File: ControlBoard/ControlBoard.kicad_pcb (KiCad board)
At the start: 2 copper layers, 144 x 106 mm, 168 parts, among them J1 PowerIn, J10 Conn_01x01, J11 Conn_01x01, J12 Conn_01x01, J13 Conn_01x01, J14 Conn_01x01, J15 Conn_01x01, J16 Conn_01x06, J17 Conn_01x06, J18 Conn_01x06, J2 UART, J3 ICSP, J4 MTR1, J5 MTR2, J6 Ultrasonic Transmitter, J7 Ultrasonic Receiver, J8 Conn_01x01, J9 Conn_01x01, Q1 2N3904, Q2 2N3904, SW1 SW_Push, U1 LM358, U10 LMT85, U11 74HC138, U12 4051, U13 4051, U2 LM358, U3 LM358, U4 LM358, U5 ATMEGA328P-PU, U6 LM7805_TO220, U7 74HC595, U8 L298D, U9 74HC595, Y1 16MHz

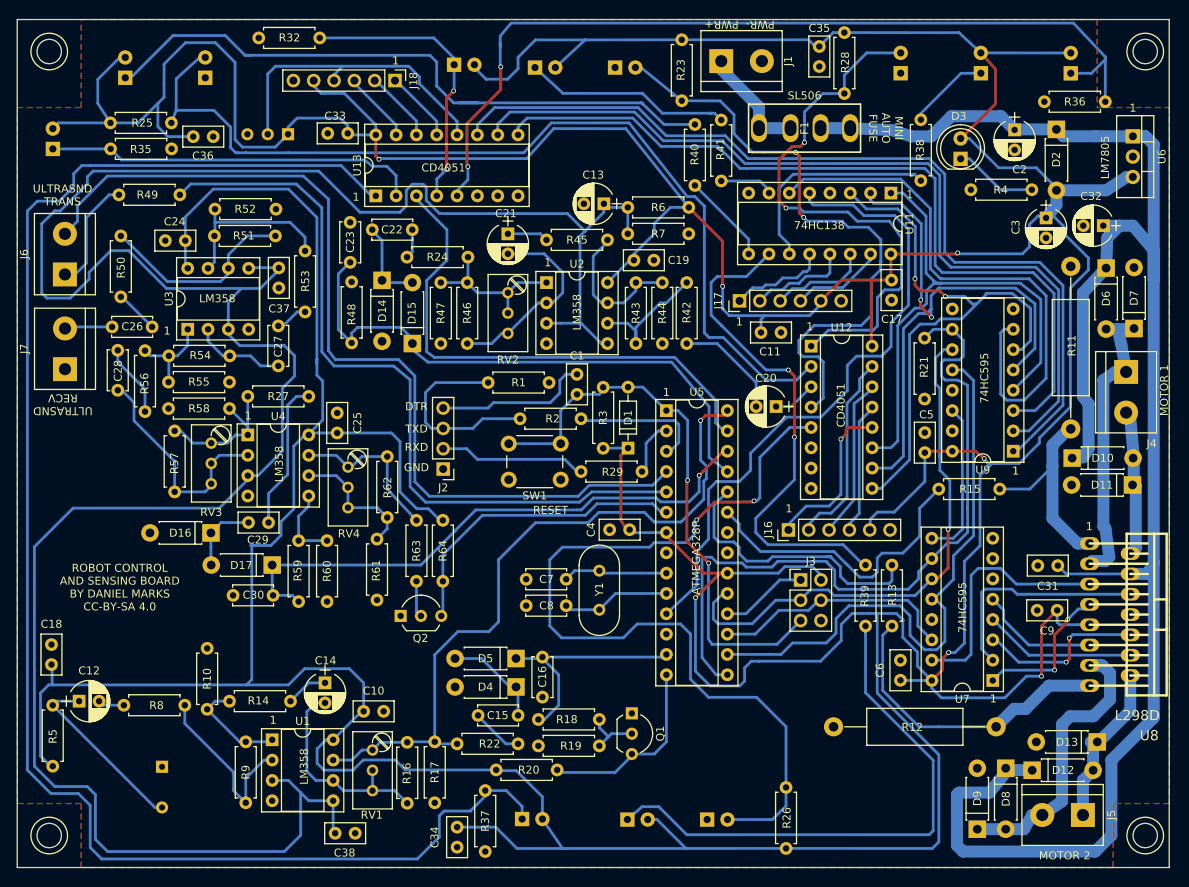
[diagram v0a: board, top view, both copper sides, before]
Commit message: Added CAD models
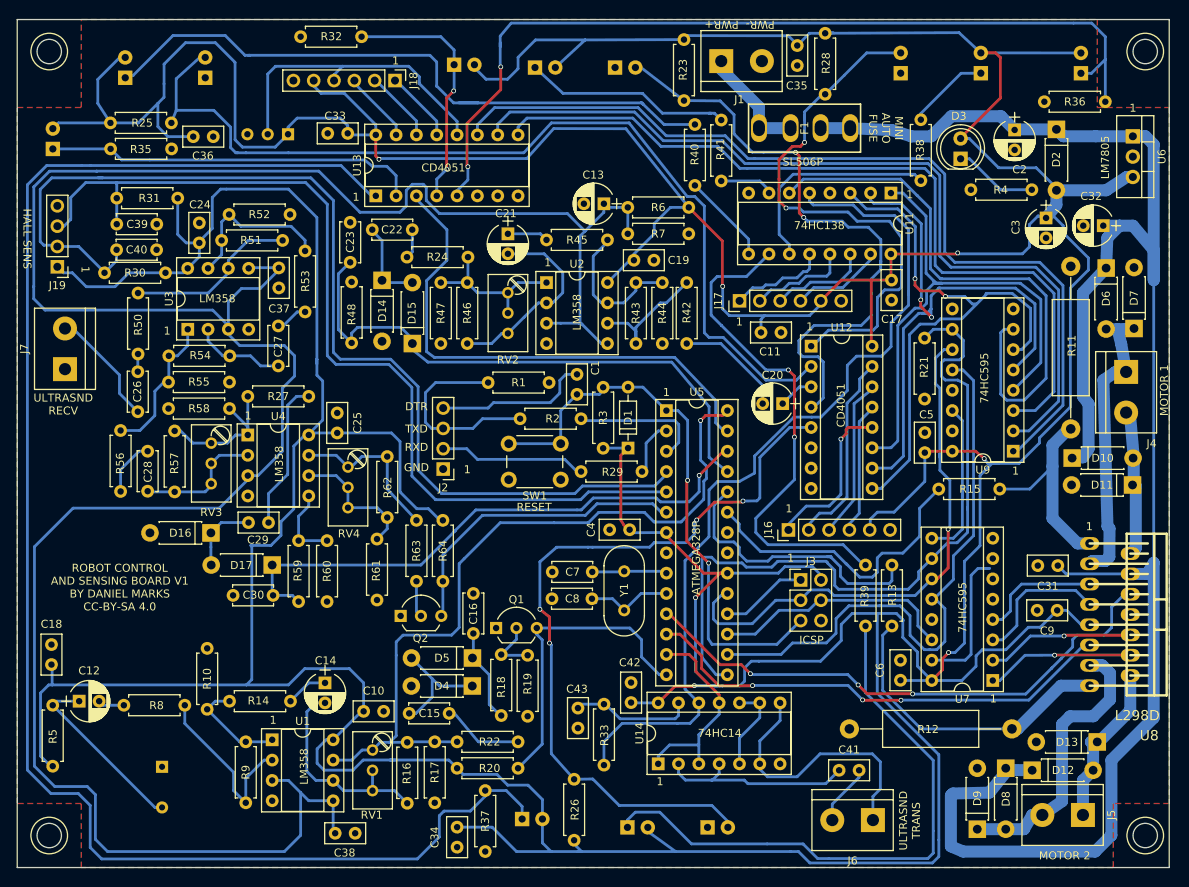
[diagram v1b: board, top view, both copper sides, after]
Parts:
- removed R49: 0R, Resistors_THT:R_Axial_DIN0207_L6.3mm_D2.5mm_P7.62mm_Horizontal
- added C39: 100 pF, Capacitors_THT:C_Disc_D5.0mm_W2.5mm_P5.00mm, F.Cu at (67.4, 64.6)
- added C40: 100 pF, Capacitors_THT:C_Disc_D5.0mm_W2.5mm_P5.00mm, F.Cu at (67.4, 67.8)
- added C41: 100 nF, Capacitors_THT:C_Disc_D5.0mm_W2.5mm_P2.50mm, F.Cu at (157.7, 132.8)
- added C42: 100 nF, Capacitors_THT:C_Disc_D5.0mm_W2.5mm_P2.50mm, F.Cu at (131.7, 124.4)
- added C43: 100 nF, Capacitors_THT:C_Disc_D5.0mm_W2.5mm_P2.50mm, F.Cu at (125.1, 125.1)
- added J19: HALLSENS, Pin_Headers:Pin_Header_Straight_1x04_Pitch2.54mm, F.Cu at (60.0, 69.9)
- added R30: 10k, Resistors_THT:R_Axial_DIN0207_L6.3mm_D2.5mm_P7.62mm_Horizontal, F.Cu at (65.9, 70.7)
- added R31: 10k, Resistors_THT:R_Axial_DIN0207_L6.3mm_D2.5mm_P7.62mm_Horizontal, F.Cu at (67.4, 61.3)
- added R33: 10k, Resistors_THT:R_Axial_DIN0207_L6.3mm_D2.5mm_P7.62mm_Horizontal, F.Cu at (128.3, 132.2)
- added U14: 74HC14, Housings_DIP:DIP-14_W7.62mm_Socket, F.Cu at (135.1, 132.0)
- F1: value SL506 -> SL506P
- R10, R29, R44: value 10k -> 1k
- moved J6 121.9 mm to (162.0, 139.1), turned to 180 degrees
- moved R26 26.5 mm to (124.6, 134.0)
- moved Q1 20.0 mm to (114.9, 115.1), turned to 0 degrees
- moved C16 15.6 mm to (112.0, 110.7), turned to 270 degrees
- moved R18 14.7 mm to (115.5, 118.4), turned to 270 degrees
- moved C15 13.6 mm to (104.0, 125.7), turned to 0 degrees
- moved C28 13.2 mm to (71.3, 98.0)
- moved R56 10.4 mm to (67.9, 98.0)
- moved R50 7.46 mm to (70.1, 73.2)
- moved C26 5.88 mm to (70.1, 83.0), turned to 270 degrees
- moved D4 5.47 mm to (111.9, 122.3)
- moved D5 5.45 mm to (111.9, 118.8)
- moved R32 5.24 mm to (90.4, 41.1)
- moved R20 4.89 mm to (117.6, 132.6)
- moved R19 3.94 mm to (118.8, 126.1), turned to 90 degrees
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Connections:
- C16 pad 2: MICPEAKOUT -> Net-(C16-Pad2)
- D5 pad 1: MICPEAKOUT -> Net-(C16-Pad2)
- J6 pad 2: ULTRATRANS1 -> Net-(C41-Pad2)
- R18 pad 2: MICPEAKOUT -> Net-(C16-Pad2)
- U5 pad 11: PHOTSIG -> MOTORPWM1
- U5 pad 12: Net-(U5-Pad12) -> MOTORPWM2
- U5 pad 13: MICPEAKOUT -> ULTRATRANS
- U5 pad 4: ULTRATRANS1 -> Net-(C40-Pad1)
- U5 pad 5: ULTRATRANS2 -> Net-(C39-Pad1)
- U7 pad 1: MTRIN2 -> MTRIN4
- U7 pad 15: MTRIN1 -> Net-(U7-Pad15)
- U7 pad 2: MTRENA -> MTRIN3
- U7 pad 3: MTRIN3 -> MTRIN2
- U7 pad 4: MTRIN4 -> MTRIN1
- U7 pad 5: MTRENB -> Net-(U7-Pad5)
- U8 pad 11: MTRENB -> MOTORPWM2
- U8 pad 6: MTRENA -> MOTORPWM1
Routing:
- net Net-(C40-Pad1): track 0.00 -> 134.1 mm
- net Net-(C39-Pad1): track 0.00 -> 119.8 mm
- net ULTRATRANS1: track 116.0 -> 0.00 mm
- net ULTRATRANS2: track 96.6 -> 0.00 mm
- net MOTORPWM1: track 0.00 -> 69.5 mm, vias 0 -> 3
- net MOTORPWM2: track 0.00 -> 60.2 mm, vias 0 -> 3
- net +5V: track 918.4 -> 957.7 mm
- net MICPEAKOUT: track 29.1 -> 0.00 mm
- net PHOTSIG: track 82.7 -> 111.0 mm
- net MTRENA: track 28.1 -> 0.00 mm
- net ULTRATRANS: track 0.00 -> 26.0 mm
- net Net-(C41-Pad1): track 0.00 -> 25.0 mm
- net Net-(J6-Pad1): track 14.2 -> 34.8 mm
- net Net-(U7-Pad15): track 0.00 -> 18.2 mm
- net MTRIN1: track 32.1 -> 16.4 mm
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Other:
- board text added: "74HC14"
- board text added: "HALL SENS"
- board text added: "ICSP"
- board text added: "ROBOT CONTROL AND SENSING BOARD V1 BY DANIEL MARKS CC-BY-SA 4.0"
- board text added: "SL506P"
- board text removed: "ROBOT CONTROL AND SENSING BOARD BY DANIEL MARKS CC-BY-SA 4.0"
- board text removed: "SL506"

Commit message: Added KeypadPI
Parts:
- added C44: 100 pF, Capacitors_THT:C_Disc_D5.0mm_W2.5mm_P5.00mm, F.Cu at (125.3, 120.9)
- added C45: 100 pF, Capacitors_THT:C_Disc_D5.0mm_W2.5mm_P5.00mm, F.Cu at (118.7, 120.9)
- added C46: 100 nF, Capacitors_THT:C_Disc_D5.0mm_W2.5mm_P2.50mm, F.Cu at (168.4, 89.2)
- added J20: Conn_01x06, Pin_Headers:Pin_Header_Straight_1x06_Pitch2.54mm, F.Cu at (178.4, 126.3)
- added J21: HALLSENS2, Pin_Headers:Pin_Header_Straight_1x04_Pitch2.54mm, F.Cu at (118.4, 115.8)
- added R34: 10k, Resistors_THT:R_Axial_DIN0207_L6.3mm_D2.5mm_P7.62mm_Horizontal, F.Cu at (128.5, 120.8)
- added R49: 10k, Resistors_THT:R_Axial_DIN0207_L6.3mm_D2.5mm_P7.62mm_Horizontal, F.Cu at (122.0, 120.9)
- added R65: 10k, Resistors_THT:R_Axial_DIN0207_L6.3mm_D2.5mm_P7.62mm_Horizontal, F.Cu at (111.7, 108.5)
- R51, R54: value 100k -> 220k
- R63: value 10k -> 1k
- moved R26 30.6 mm to (155.2, 134.8)
- moved C16 17.8 mm to (94.8, 115.2), turned to 0 degrees
- moved R10 11.2 mm to (68.3, 121.5), turned to 0 degrees
- moved C14 11.1 mm to (82.5, 120.2), turned to 0 degrees
- moved C43 9.40 mm to (121.2, 133.6), turned to 90 degrees
- moved R18 9.19 mm to (111.0, 126.4), turned to 90 degrees
- moved C15 7.47 mm to (96.5, 125.3)
- moved D4 7.45 mm to (104.4, 122.0)
- moved D5 7.44 mm to (104.5, 118.5)
- moved C10 6.41 mm to (92.0, 124.2), turned to 180 degrees
- moved C41 5.34 mm to (153.9, 129.1), turned to 270 degrees
- moved R12 3.70 mm to (177.6, 130.9)
- moved R22 3.62 mm to (107.8, 126.4), turned to 90 degrees
- moved R14 3.36 mm to (78.2, 124.7)
- moved R19 3.29 mm to (117.6, 129.2), turned to 180 degrees
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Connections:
- J3 pad 1: MISO -> MICTHR
- Q1 pad 3: MICTHR -> Net-(Q1-Pad3)
- R20 pad 1: MICTHR -> Net-(Q1-Pad3)
- R21 pad 1: CLROUT -> +5V
- R21 pad 2: GND -> CLROUT
- U5 pad 14: MICTHR -> Net-(C45-Pad1)
- U5 pad 15: CLROUT -> Net-(C44-Pad1)
- U5 pad 18: MISO -> MICTHR
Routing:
- net +5V: track 957.7 -> 1020.9 mm
- net CLROUT: track 91.9 -> 51.2 mm
- net Net-(C44-Pad1): track 0.00 -> 31.4 mm, vias 0 -> 2
- net Net-(Q1-Pad3): track 0.00 -> 29.6 mm
- net Net-(PT2-Pad2): track 96.4 -> 124.1 mm, vias 4 -> 2
- net Net-(C45-Pad1): track 0.00 -> 26.6 mm
- net Net-(J20-Pad4): track 0.00 -> 23.8 mm
- net Net-(J20-Pad3): track 0.00 -> 20.2 mm
- net Net-(J20-Pad2): track 0.00 -> 17.5 mm
- net MICOUT: track 95.3 -> 111.3 mm
- net Net-(Q1-Pad2): track 7.44 -> 18.4 mm
- net MISO: track 10.9 -> 0.00 mm
- net Net-(J20-Pad5): track 18.2 -> 9.03 mm
- net Net-(R12-Pad1): track 39.3 -> 46.5 mm
- net Net-(C43-Pad1): track 15.3 -> 22.2 mm
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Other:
- board text added: "HALL SENS 2"

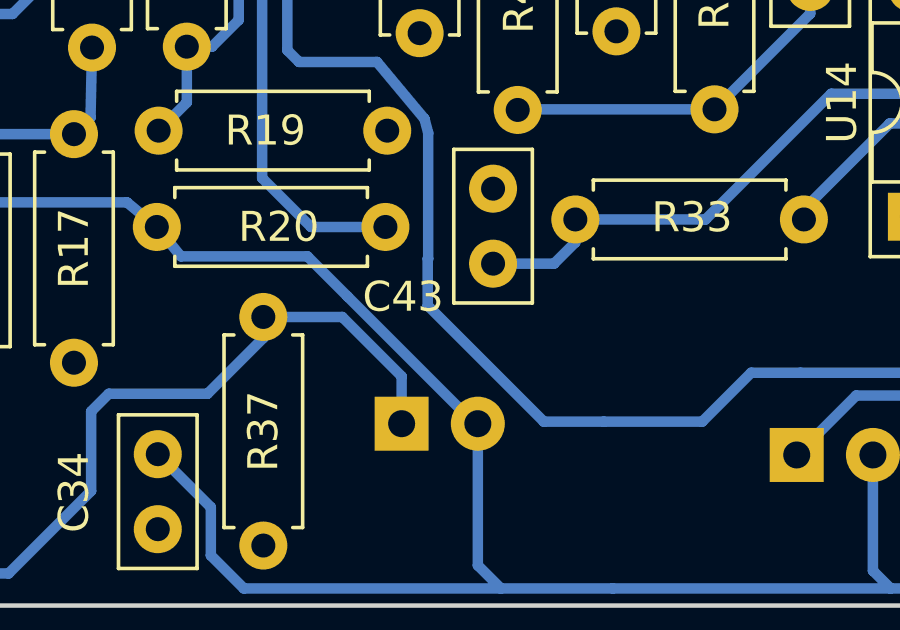
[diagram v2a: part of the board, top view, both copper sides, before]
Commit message: Added audio input and output to keypad PCB
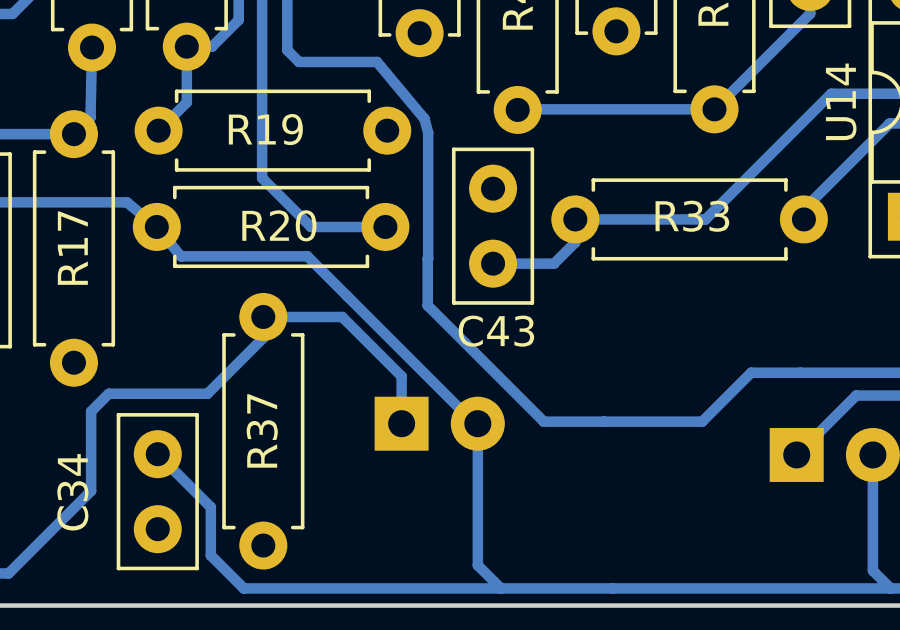
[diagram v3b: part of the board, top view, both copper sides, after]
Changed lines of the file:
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@@
     (links 409)
     (no_connects 0)
-    (area 54.924999 38.924999 199.075001 145.075001)
+    (area 54.252381 38.749 200.74762 145.335)
     (thickness 1.6)
     (drawings 54)
@@
   )
   (setup
-    (last_trace_width 0.35)
+    (last_trace_width 0.25)
     (user_trace_width 0.35)
     (user_trace_width 0.5)
@@
     (descr "C, Disc series, Radial, pin pitch=2.50mm, , diameter*width=5*2.5mm^2, Capacitor, http://cdn-reichelt.de/documents/datenblatt/B300/DS_KERKO_TC.pdf")
     (tags "C Disc series Radial pin pitch 2.50mm  diameter 5mm width 2.5mm Capacitor")
-    (fp_text reference C43 (at -1.106 -2.998 180) (layer F.SilkS)
+    (fp_text reference C43 (at -2.286 0.127 180) (layer F.SilkS)
       (effects (font (size 1 1) (thickness 0.15)))
     )

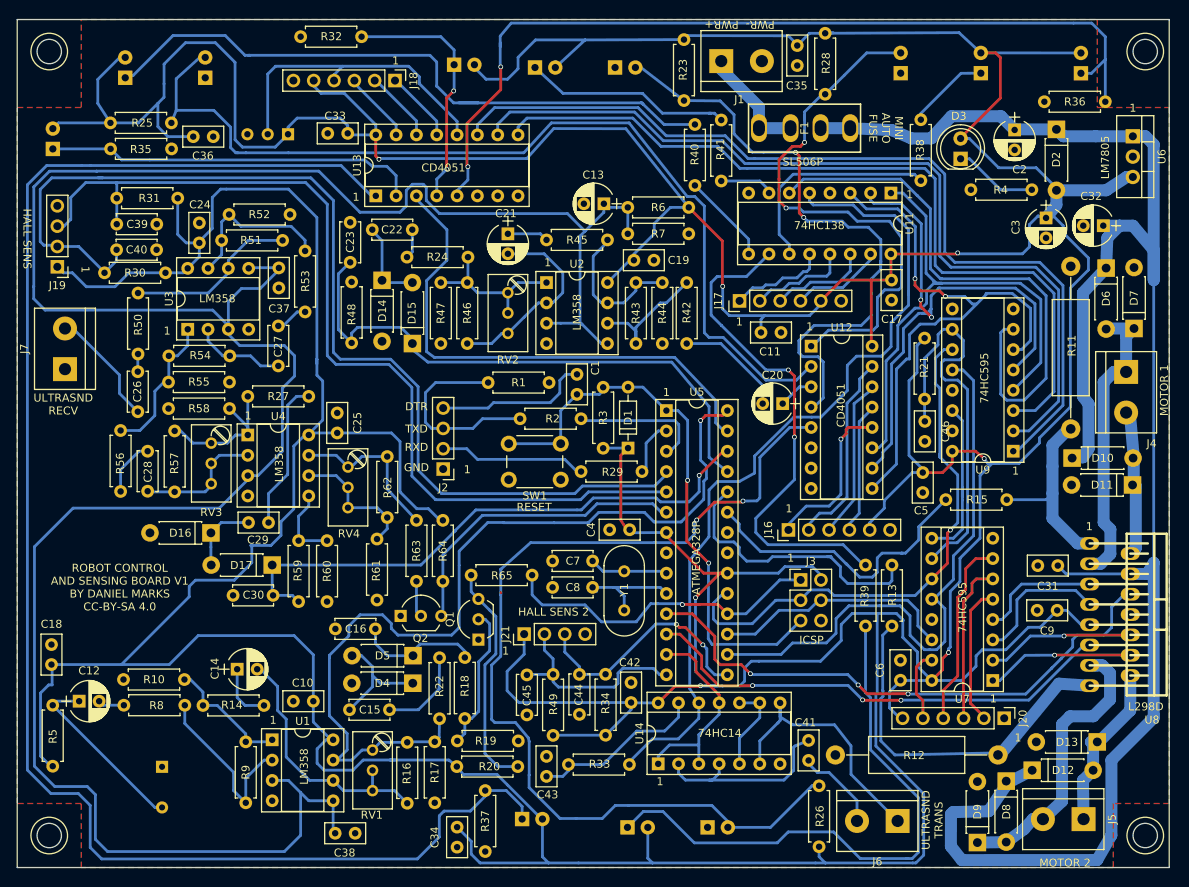
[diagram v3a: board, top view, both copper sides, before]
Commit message: Added second microphone to keypad
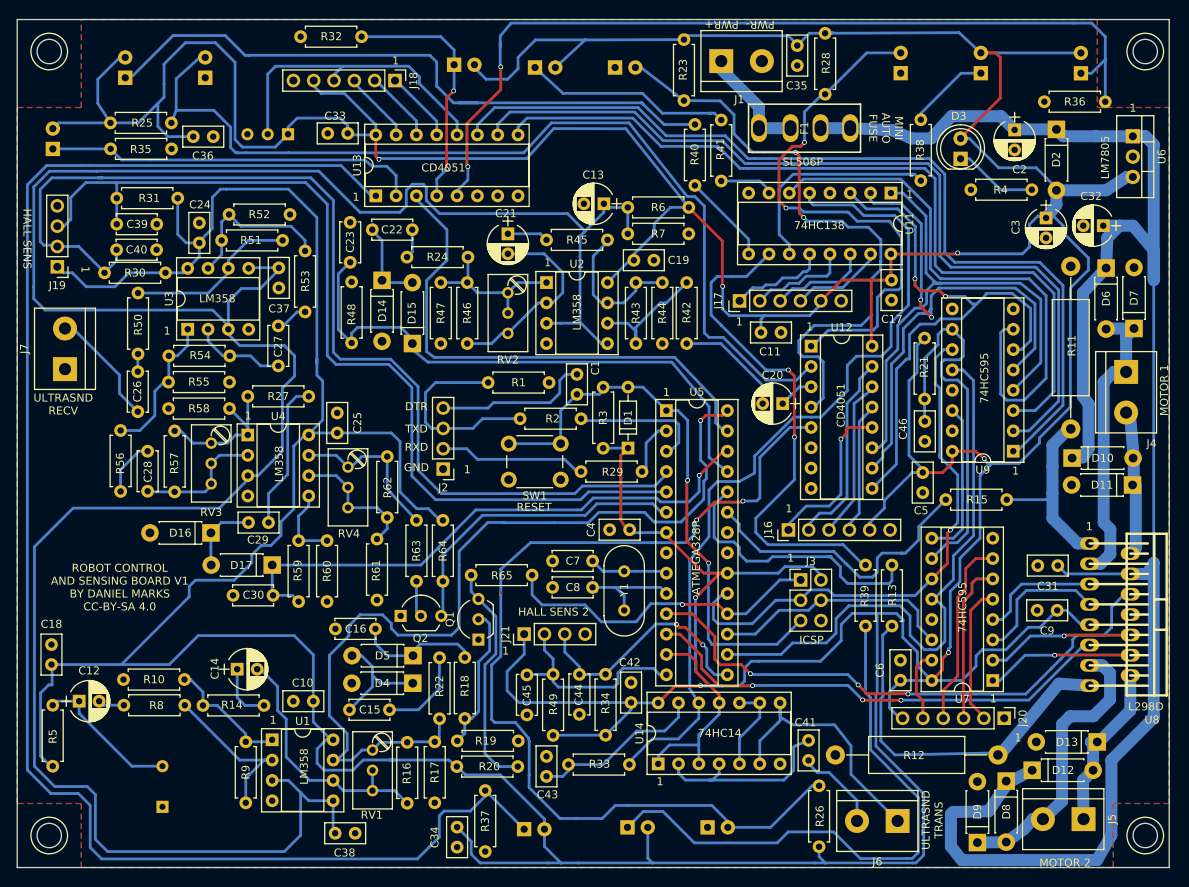
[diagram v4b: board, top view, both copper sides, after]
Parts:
- moved PDT1 1.30 mm to (118.4, 140.2)
- moved MK1 0.09 mm to (73.2, 134.9), turned to 0 degrees
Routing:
- net Net-(C12-Pad1): track 22.6 -> 18.2 mm
- net Net-(R8-Pad1): track 22.6 -> 21.1 mm

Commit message: A few fixes
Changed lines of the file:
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@@
     (thickness 1.6)
     (drawings 54)
-    (tracks 1942)
+    (tracks 1943)
     (zones 0)
     (modules 185)
@@
   )
   (setup
-    (last_trace_width 0.35)
+    (last_trace_width 1.5)
     (user_trace_width 0.35)
     (user_trace_width 0.5)
@@
   (segment (start 123.568 83.352) (end 122.82 84.1) (width 0.35) (layer B.Cu) (net 2))
   (segment (start 124.718 83.102) (end 124.968 83.352) (width 0.35) (layer B.Cu) (net 2) (status 30))
+  (segment (start 197.06 107) (end 197.06 71.575) (width 1.5) (layer B.Cu) (net 3))
   (segment (start 194.13 108.3) (end 186.11 108.3) (width 0.35) (layer B.Cu) (net 3))
   (segment (start 186.11 108.3) (end 185.07 107.26) (width 0.35) (layer B.Cu) (net 3))
@@
   (segment (start 185.764 53.594) (end 184.9 52.73) (width 1.5) (layer B.Cu) (net 3))
   (segment (start 197.06 71.575) (end 197.06 54.635) (width 1.5) (layer B.Cu) (net 3))
-  (segment (start 196.019 53.594) (end 194.45 53.6) (width 1.5) (layer B.Cu) (net 3) (status 20))
   (segment (start 197.06 54.635) (end 196.019 53.594) (width 1.5) (layer B.Cu) (net 3))
+  (segment (start 196.019 53.594) (end 194.45 53.6) (width 1.5) (layer B.Cu) (net 3) (status 20))
   (segment (start 189.794 53.594) (end 194.45 53.6) (width 1.5) (layer B.Cu) (net 3) (status 20))
   (segment (start 197.06 125.984) (end 197.06 126.282) (width 1.5) (layer B.Cu) (net 3))
@@
   (segment (start 173.067762 144.070539) (end 189.988 144.062) (width 1.5) (layer B.Cu) (net 3))
   (segment (start 189.988 144.062) (end 191.77 140.97) (width 1.5) (layer B.Cu) (net 3))
-  (segment (start 197.06 125.984) (end 197.06 106.91) (width 1.5) (layer B.Cu) (net 3))
+  (segment (start 197.06 125.984) (end 197.06 107) (width 1.5) (layer B.Cu) (net 3))
+  (segment (start 197.06 107) (end 197.06 106.91) (width 1.5) (layer B.Cu) (net 3))
   (segment (start 181.864 132.842) (end 178.832 134.412) (width 1.5) (layer B.Cu) (net 3) (status 20))
   (segment (start 178.832 134.412) (end 178.62 134.2) (width 1.5) (layer B.Cu) (net 3) (status 30))
   (segment (start 194.13 108.3) (end 196.25 108.3) (width 1.5) (layer B.Cu) (net 3))
   (segment (start 197.06 67.84) (end 194.47 64.77) (width 1.5) (layer B.Cu) (net 3))
-  (segment (start 197.06 106.91) (end 197.06 71.575) (width 0.35) (layer B.Cu) (net 3))
+  (segment (start 194.47 64.77) (end 192.786 64.77) (width 1.5) (layer B.Cu) (net 3))
   (segment (start 197.06 71.575) (end 197.06 67.84) (width 1.5) (layer B.Cu) (net 3))
   (segment (start 196.25 108.3) (end 197.06 106.91) (width 1.5) (layer B.Cu) (net 3))
@@
   (segment (start 191.262 66.294) (end 192.786 64.77) (width 1.5) (layer B.Cu) (net 3))
   (segment (start 194.45 53.6) (end 195.212 53.6) (width 1.5) (layer B.Cu) (net 3) (status 30))
-  (segment (start 194.47 64.77) (end 192.786 64.77) (width 1.5) (layer B.Cu) (net 3))
   (segment (start 192.786 64.77) (end 190.754 64.77) (width 1.5) (layer B.Cu) (net 3))
   (segment (start 185.07 107.26) (end 185.47 107.26) (width 0.35) (layer B.Cu) (net 3) (status 30))

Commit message: JLCPCB order 2021-10-03
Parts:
- added C47: 100 uF, Capacitors_THT:CP_Radial_D5.0mm_P2.50mm, F.Cu at (72.1, 111.2)
- added J22: PowerIn, Connectors_Terminal_Blocks:TerminalBlock_bornier-2_P5.08mm, F.Cu at (59.4, 116.1)
- R23, R25, R26, R28: value 1k -> 10k
- moved R5 10.2 mm to (59.4, 122.2), turned to 270 degrees
- moved C18 8.66 mm to (67.4, 116.7)
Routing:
- net +5V: track 1020.9 -> 1088.6 mm
- net Net-(C12-Pad1): track 18.2 -> 21.1 mm
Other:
- board text added: "+5V"
